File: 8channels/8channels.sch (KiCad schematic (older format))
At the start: 6 parts, among them P1 PCIEX1_02X18, P2 PCIEX1_02X18, U1 SN74CB3Q3251PWR, U2 SN74CB3Q3251PWR, U3 SN74CB3Q3251PWR, U4 SN74CB3Q3251PWR

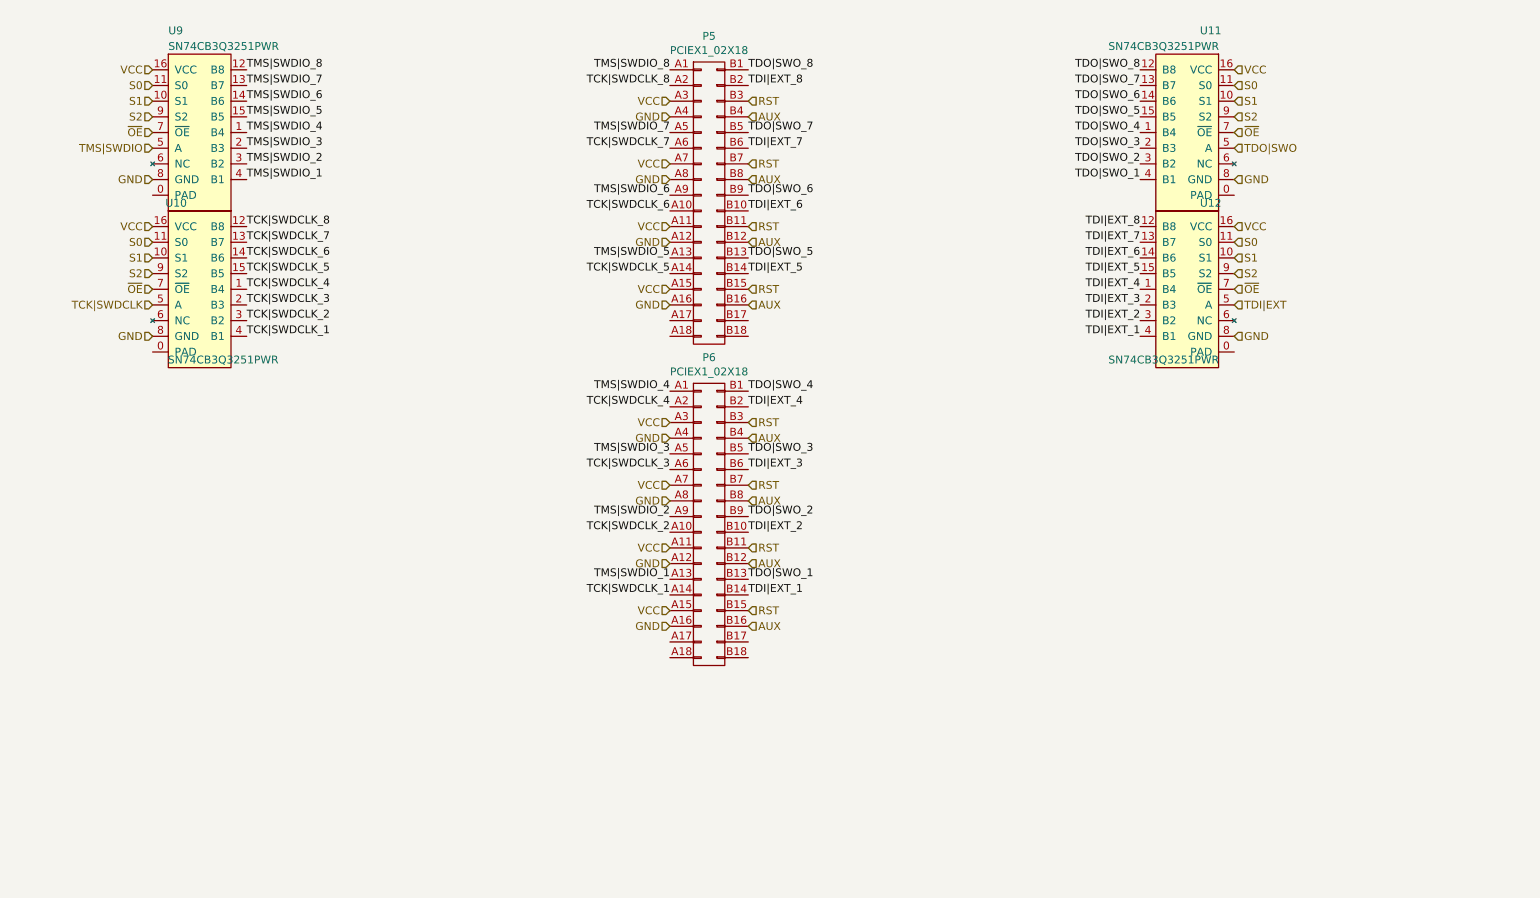
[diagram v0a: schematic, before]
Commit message: Restructure files
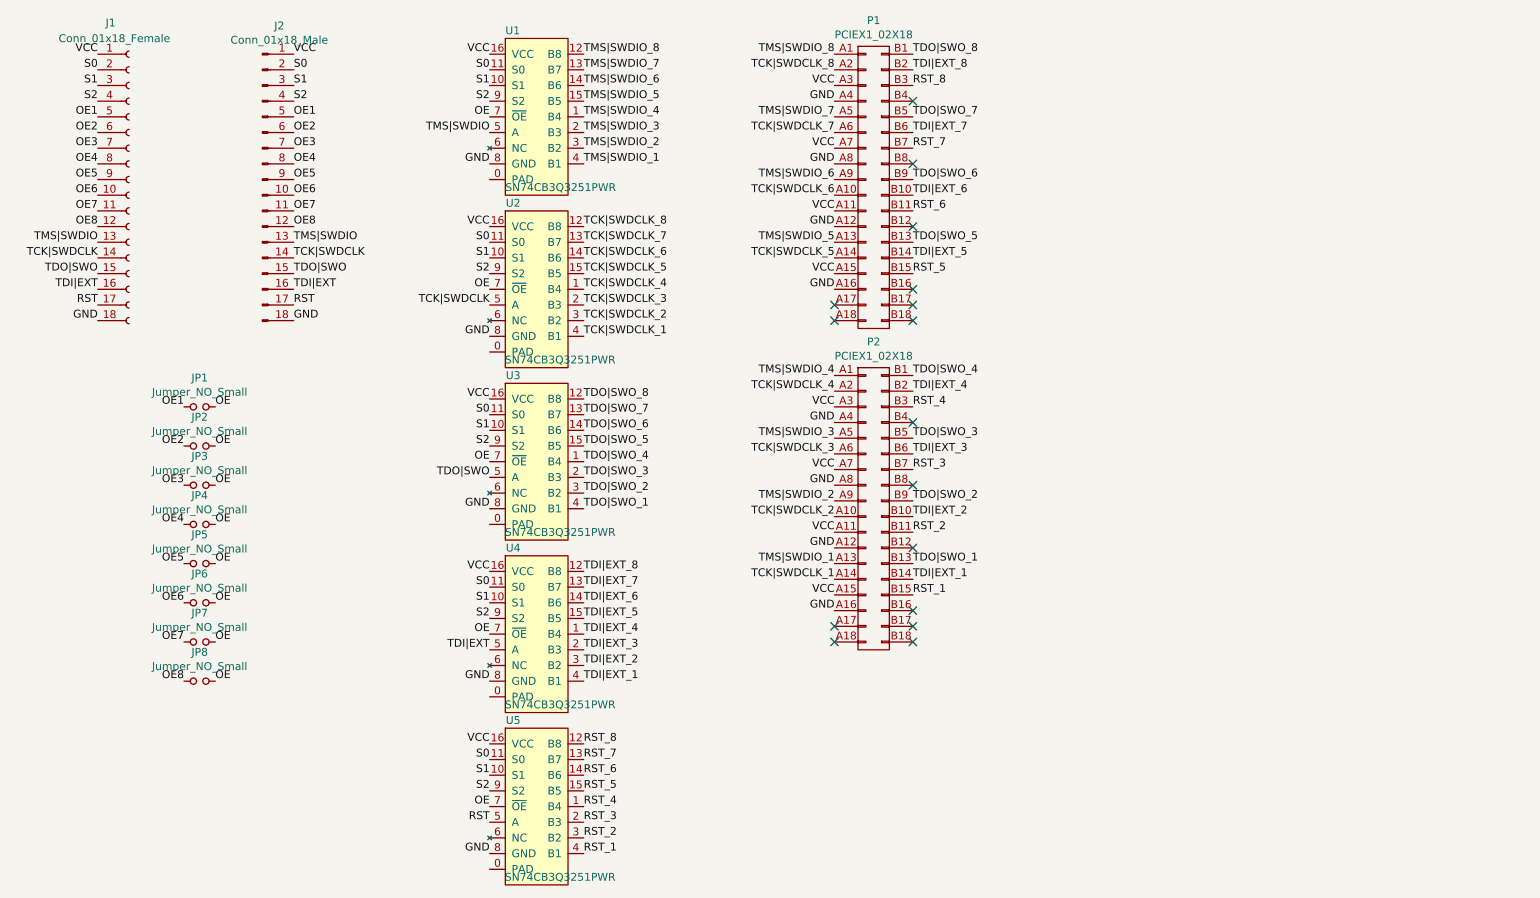
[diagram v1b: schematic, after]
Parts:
- added J1: Conn_01x18_Female, Connector_PinSocket_2.54mm:PinSocket_1x18_P2.54mm_Horizontal, symbol Connector:Conn_01x18_Female
- added J2: Conn_01x18_Male, Connector_PinHeader_2.54mm:PinHeader_1x18_P2.54mm_Horizontal, symbol Connector:Conn_01x18_Male
- added JP1, JP2, JP3, JP4, JP5, JP6, JP7, JP8: Jumper_NO_Small, Jumper:SolderJumper-2_P1.3mm_Open_Pad1.0x1.5mm, symbol Device:Jumper_NO_Small
- added U5: SN74CB3Q3251PWR, probe-rs-hive:R-PVQFN-N16, symbol probe-rs-hive:SN74CB3Q3251PWR
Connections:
- net GND: now also J1.18 (Pin_18), J2.18 (Pin_18), U5.8 (GND)
- net RST: now also J1.17 (Pin_17), J2.17 (Pin_17), U5.5 (A); no longer P1.B11 (P22), P1.B15 (P30), P1.B3 (P6), P1.B7 (P14), P2.B11 (P22), P2.B15 (P30), P2.B3 (P6), P2.B7 (P14)
- net S0: now also J1.2 (Pin_2), J2.2 (Pin_2), U5.11 (S0)
- net S1: now also J1.3 (Pin_3), J2.3 (Pin_3), U5.10 (S1)
- net S2: now also J1.4 (Pin_4), J2.4 (Pin_4), U5.9 (S2)
- net TCK|SWDCLK: now also J1.14 (Pin_14), J2.14 (Pin_14)
- net TDI|EXT: now also J1.16 (Pin_16), J2.16 (Pin_16)
- net TDO|SWO: now also J1.15 (Pin_15), J2.15 (Pin_15)
- net TMS|SWDIO: now also J1.13 (Pin_13), J2.13 (Pin_13)
- net VCC: now also J1.1 (Pin_1), J2.1 (Pin_1), U5.16 (VCC)
- removed net AUX: P1.B12 (P24), P1.B16 (P32), P1.B4 (P8), P1.B8 (P16), P2.B12 (P24), P2.B16 (P32), P2.B4 (P8), P2.B8 (P16)
- net ~OE renamed OE
- net OE: now also JP1.2, JP2.2, JP3.2, JP4.2, JP5.2, JP6.2, JP7.2, JP8.2, U5.7 (~OE)
- new net OE1: J1.5 (Pin_5), J2.5 (Pin_5), JP1.1
- new net OE2: J1.6 (Pin_6), J2.6 (Pin_6), JP2.1
- new net OE3: J1.7 (Pin_7), J2.7 (Pin_7), JP3.1
- new net OE4: J1.8 (Pin_8), J2.8 (Pin_8), JP4.1
- new net OE5: J1.9 (Pin_9), J2.9 (Pin_9), JP5.1
- new net OE6: J1.10 (Pin_10), J2.10 (Pin_10), JP6.1
- new net OE7: J1.11 (Pin_11), J2.11 (Pin_11), JP7.1
- new net OE8: J1.12 (Pin_12), J2.12 (Pin_12), JP8.1
- new net RST_1: P2.B15 (P30), U5.4 (B1)
- new net RST_2: P2.B11 (P22), U5.3 (B2)
- new net RST_3: P2.B7 (P14), U5.2 (B3)
- new net RST_4: P2.B3 (P6), U5.1 (B4)
- new net RST_5: P1.B15 (P30), U5.15 (B5)
- new net RST_6: P1.B11 (P22), U5.14 (B6)
- new net RST_7: P1.B7 (P14), U5.13 (B7)
- new net RST_8: P1.B3 (P6), U5.12 (B8)
- no-connect marks 0 -> 16

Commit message: Add caps & get rid of the jumpers & add two more GND lanes to the connector & remove two OE select signals
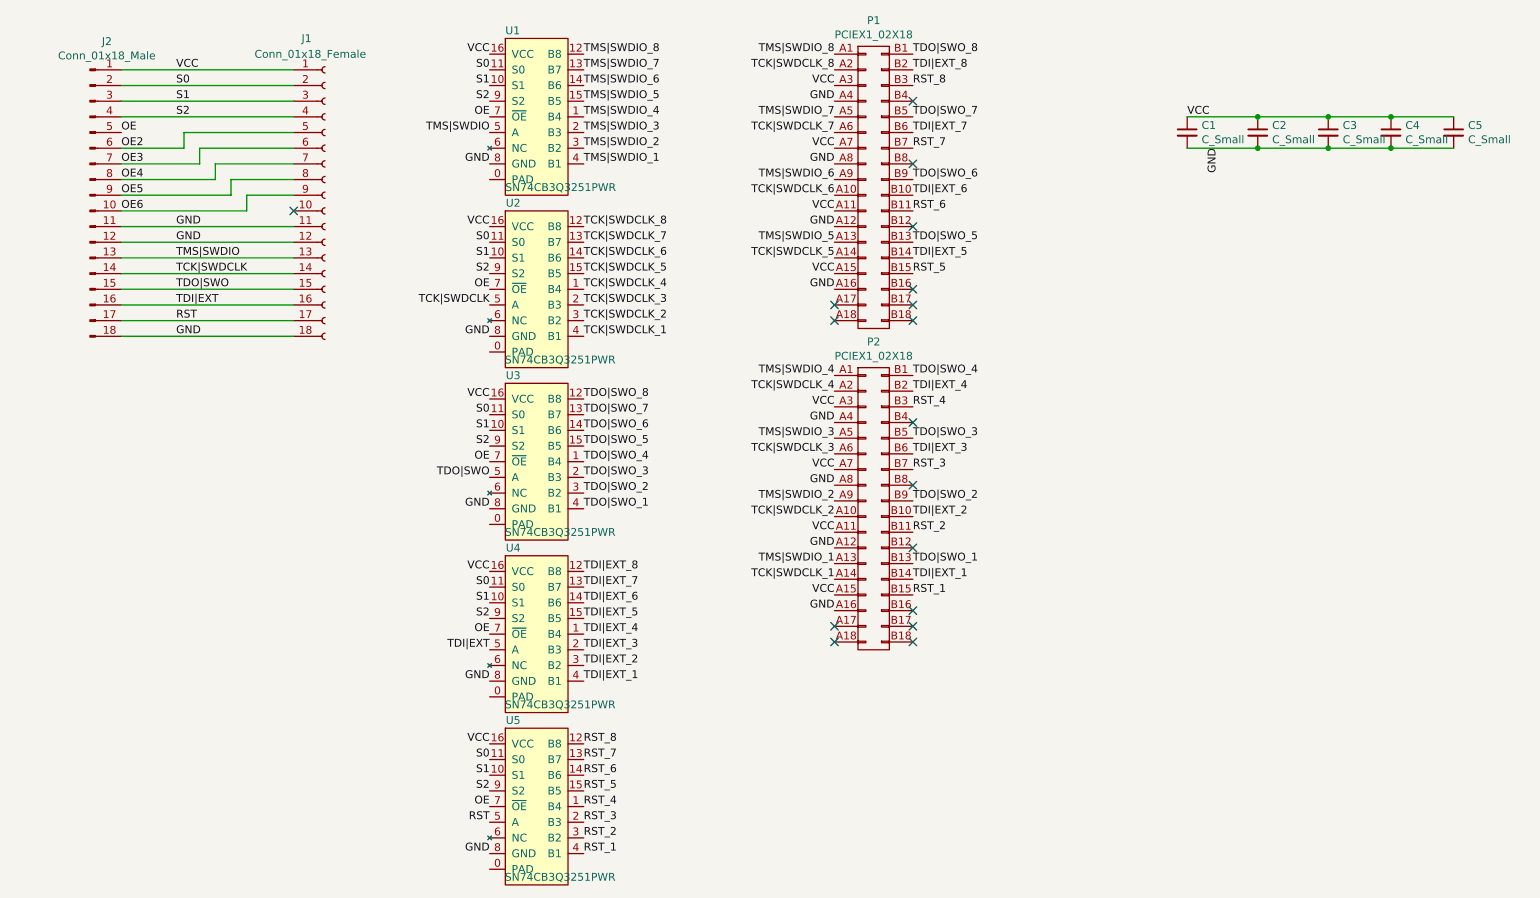
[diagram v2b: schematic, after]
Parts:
- removed JP1, JP2, JP3, JP4, JP5, JP6, JP7, JP8: Jumper_NO_Small, Jumper:SolderJumper-2_P1.3mm_Open_Pad1.0x1.5mm, symbol Device:Jumper_NO_Small
- added C1, C2, C3, C4, C5: C_Small, Capacitor_SMD:C_0402_1005Metric, symbol Device:C_Small
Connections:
- net OE7 is gone; now on net GND: J1.11 (Pin_11), J2.11 (Pin_11)
- net OE8 is gone; now on net GND: J1.12 (Pin_12), J2.12 (Pin_12)
- net GND: now also C1.2, C2.2, C3.2, C4.2, C5.2
- net OE: now also J2.5 (Pin_5)
- net OE2: now also J1.5 (Pin_5); no longer J1.6 (Pin_6)
- net OE3: now also J1.6 (Pin_6); no longer J1.7 (Pin_7)
- net OE4: now also J1.7 (Pin_7); no longer J1.8 (Pin_8)
- net OE5: now also J1.8 (Pin_8); no longer J1.9 (Pin_9)
- net OE6: now also J1.9 (Pin_9); no longer J1.10 (Pin_10)
- net VCC: now also C1.1, C2.1, C3.1, C4.1, C5.1
- removed net OE1: J1.5 (Pin_5), J2.5 (Pin_5)
- no-connect marks 16 -> 17
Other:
- moved on the sheet: J1, J2

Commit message: Remade 8channel board
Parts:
- J1: footprint Connector_PinSocket_2.54mm:PinSocket_1x18_P2.54mm_Horizontal -> Connector_PinSocket_2.54mm:PinSocket_2x10_P2.54mm_Horizontal; symbol Connector:Conn_01x18_Female -> Connector:Conn_01x20_Female
- J2: footprint Connector_PinHeader_2.54mm:PinHeader_1x18_P2.54mm_Horizontal -> Connector_PinHeader_2.54mm:PinHeader_2x10_P2.54mm_Horizontal; symbol Connector:Conn_01x18_Male -> Connector:Conn_01x20_Male
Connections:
- net GND: now also J1.13 (Pin_13), J1.14 (Pin_14), J1.20 (Pin_20), J2.13 (Pin_13), J2.14 (Pin_14), J2.20 (Pin_20), U1.0 (PAD), U2.0 (PAD), U3.0 (PAD), U4.0 (PAD), U5.0 (PAD); no longer J1.11 (Pin_11), J1.12 (Pin_12), J1.18 (Pin_18), J2.11 (Pin_11), J2.12 (Pin_12), J2.18 (Pin_18)
- net RST: now also J1.19 (Pin_19), J2.19 (Pin_19); no longer J1.17 (Pin_17), J2.17 (Pin_17)
- net TCK|SWDCLK: now also J1.16 (Pin_16), J2.16 (Pin_16); no longer J1.14 (Pin_14), J2.14 (Pin_14)
- net TDI|EXT: now also J1.18 (Pin_18), J2.18 (Pin_18); no longer J1.16 (Pin_16), J2.16 (Pin_16)
- net TDO|SWO: now also J1.17 (Pin_17), J2.17 (Pin_17); no longer J1.15 (Pin_15), J2.15 (Pin_15)
- net TMS|SWDIO: now also J1.15 (Pin_15), J2.15 (Pin_15); no longer J1.13 (Pin_13), J2.13 (Pin_13)
- net OE7: now reaches J1.10 (Pin_10)
- net OE7: now also J2.11 (Pin_11)
- net VCC renamed +3V3
- new net OE8: J1.11 (Pin_11), J2.12 (Pin_12)

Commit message: Now with LDO per 8 channel board
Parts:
- added C101, C102: 1u, Capacitor_SMD:C_0402_1005Metric, symbol Device:C_Small
- added U101: MIC5353-3.3YMT, Package_DFN_QFN:MLF-6-1EP_1.6x1.6mm_P0.5mm_EP0.5x1.26mm, symbol Regulator_Linear:MIC5353-3.3YMT
- C1, C2, C3, C4, C5: value C_Small -> 0.1u
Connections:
- net +3V3: now also C102.1, U101.4 (VOUT); no longer J1.1 (Pin_1), J2.1 (Pin_1)
- net GND: now also C101.2, C102.2, U101.2 (GND), U101.7 (GND)
- net OE: now also U101.1 (EN)
- new net +5V: C101.1, J1.1 (Pin_1), J2.1 (Pin_1), U101.3 (VIN)
- no-connect marks 17 -> 18

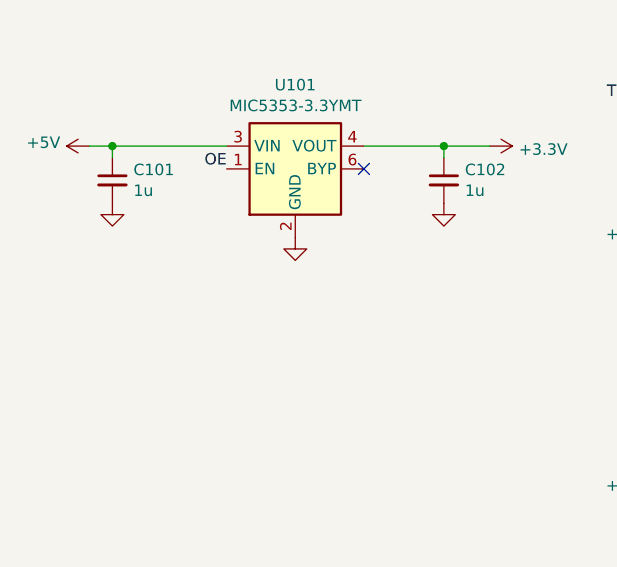
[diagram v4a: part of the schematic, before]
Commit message: Add OE pulldown
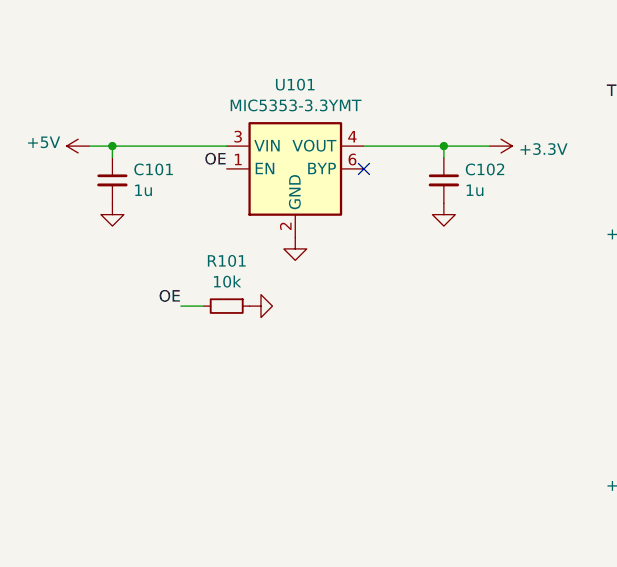
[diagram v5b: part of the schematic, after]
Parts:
- added R101: 10k, Resistor_SMD:R_0402_1005Metric, symbol Device:R_Small
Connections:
- net GND: now also R101.1
- net OE: now also R101.2
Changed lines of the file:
@@
 Wire Wire Line
 	1350 2150 2300 2150
+Text Label 1350 4450 2    50   ~ 0
+OE
+$Comp
+L Device:R_Small R101
+U 1 1 5FB98C95
+P 1550 4450
+F 0 "R101" V 1354 4450 50  0000 C CNN
+F 1 "10k" V 1445 4450 50  0000 C CNN
+F 2 "Resistor_SMD:R_0402_1005Metric" H 1550 4450 50  0001 C CNN
+F 3 "~" H 1550 4450 50  0001 C CNN
+	1    1550 4450
+	0    1    1    0
+$EndComp
+Wire Wire Line
+	1450 4450 1350 4450
+$Comp
+L power:GND #PWR0141
+U 1 1 5FB9AAEF
+P 1650 4450
+F 0 "#PWR0141" H 1650 4200 50  0001 C CNN
+F 1 "GND" H 1655 4277 50  0001 C CNN
+F 2 "" H 1650 4450 50  0001 C CNN
+F 3 "" H 1650 4450 50  0001 C CNN
+	1    1650 4450
+	0    -1   -1   0
+$EndComp
 $EndSCHEMATC

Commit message: Add cache files
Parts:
- added H1, H2, H3, H4: MountingHole, MountingHole:MountingHole_3.2mm_M3, symbol Mechanical:MountingHole
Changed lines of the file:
@@
 	0    -1   -1   0
 $EndComp
+$Comp
+L Mechanical:MountingHole H1
+U 1 1 60E4E339
+P 9350 3250
+F 0 "H1" H 9450 3296 50  0000 L CNN
+F 1 "MountingHole" H 9450 3205 50  0000 L CNN
+F 2 "MountingHole:MountingHole_3.2mm_M3" H 9350 3250 50  0001 C CNN
+F 3 "~" H 9350 3250 50  0001 C CNN
+	1    9350 3250
+	1    0    0    -1
+$EndComp
+$Comp
+L Mechanical:MountingHole H2
+U 1 1 60E4F26C
+P 9350 3500
+F 0 "H2" H 9450 3546 50  0000 L CNN
+F 1 "MountingHole" H 9450 3455 50  0000 L CNN
+F 2 "MountingHole:MountingHole_3.2mm_M3" H 9350 3500 50  0001 C CNN
+F 3 "~" H 9350 3500 50  0001 C CNN
+	1    9350 3500
+	1    0    0    -1
+$EndComp
+$Comp
+L Mechanical:MountingHole H3
+U 1 1 60E50742
+P 9350 3750
+F 0 "H3" H 9450 3796 50  0000 L CNN
+F 1 "MountingHole" H 9450 3705 50  0000 L CNN
+F 2 "MountingHole:MountingHole_3.2mm_M3" H 9350 3750 50  0001 C CNN
+F 3 "~" H 9350 3750 50  0001 C CNN
+	1    9350 3750
+	1    0    0    -1
+$EndComp
+$Comp
+L Mechanical:MountingHole H4
+U 1 1 60E51C3B
+P 9350 4000
+F 0 "H4" H 9450 4046 50  0000 L CNN
+F 1 "MountingHole" H 9450 3955 50  0000 L CNN
+F 2 "MountingHole:MountingHole_3.2mm_M3" H 9350 4000 50  0001 C CNN
+F 3 "~" H 9350 4000 50  0001 C CNN
+	1    9350 4000
+	1    0    0    -1
+$EndComp
 $EndSCHEMATC
